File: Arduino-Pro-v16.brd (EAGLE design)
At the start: 100 x 80 mm, 36 parts, among them IC1 ATMEGA1281-16AU, IC2 MCP170312MB, J1 FTDI Basic Programmer

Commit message: Started ordering the layout of the board
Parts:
- removed FRAME1: FRAME-LETTER, SparkFun-Aesthetics:CREATIVE_COMMONS
- moved IC2 378.9 mm to (14.0, 68.6)
- moved JTAG_CONNECTOR 376.8 mm to (39.4, 69.8), turned to 180 degrees
- moved J2 370.5 mm to (62.2, 33.0)
- moved C4 361.5 mm to (45.7, 38.1), turned to 90 degrees
- moved J1 357.2 mm to (2.54, 50.8), turned to 90 degrees
- moved U$1 342.5 mm to (52.1, 41.9)
- moved R5 271.5 mm to (44.5, 41.9), turned to 180 degrees
- moved R4 270.4 mm to (44.5, 44.5), turned to 180 degrees
- moved R2 269.2 mm to (44.5, 47.0), turned to 180 degrees
- moved R1 268.1 mm to (44.5, 49.5), turned to 180 degrees
- moved LED5 263.6 mm to (40.6, 49.5), turned to 270 degrees
- moved LED4 259.6 mm to (40.6, 47.0), turned to 270 degrees
- moved LED3 255.7 mm to (40.6, 44.5), turned to 270 degrees
- moved T1 255.6 mm to (62.2, 38.1)
- moved D1 252.8 mm to (61.0, 43.2)
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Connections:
- removed net N$18: PWM3.1
- removed net N$19: PWM3.2
- removed net N$20: PWM3.3
- net PWM3A: now also PWM3.1
- net PWM3B: now also PWM3.2
- net PWM3C: now also PWM3.3

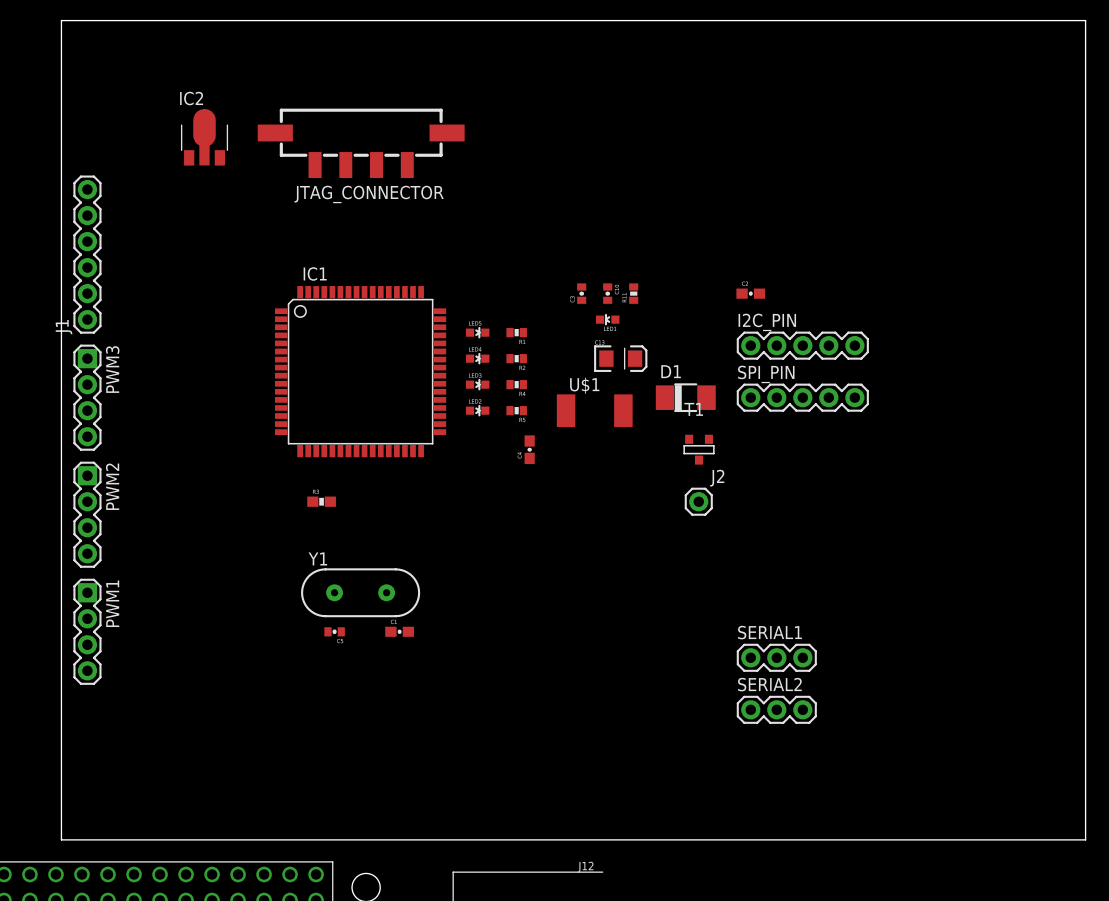
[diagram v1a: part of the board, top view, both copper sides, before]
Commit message: continued working on board layout, added ground plan polygon
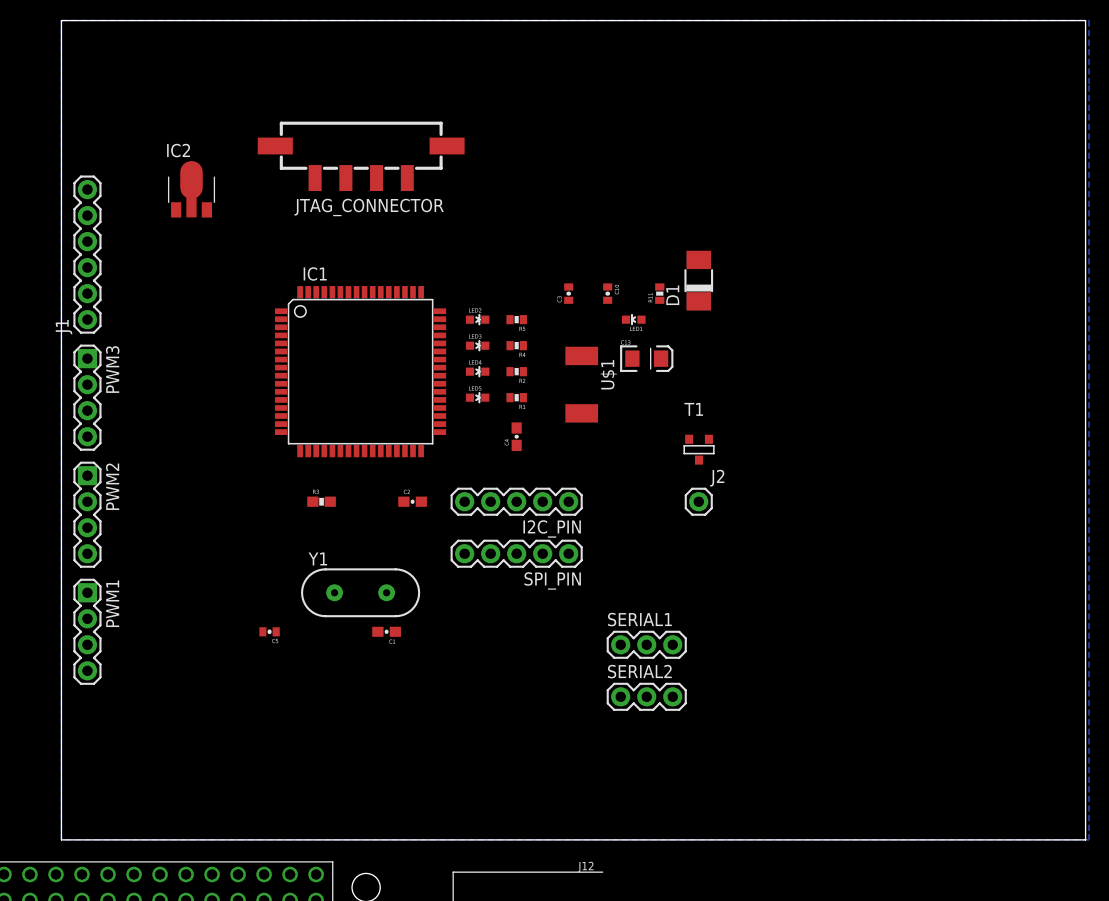
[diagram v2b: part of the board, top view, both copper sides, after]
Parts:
- moved C2 38.8 mm to (34.3, 33.0)
- moved SPI_PIN 23.4 mm to (49.5, 27.9), turned to 180 degrees
- moved I2C_PIN 23.4 mm to (49.5, 33.0), turned to 180 degrees
- moved SERIAL1 12.8 mm to (54.6, 19.1)
- moved SERIAL2 12.8 mm to (54.6, 14.0)
- moved D1 11.5 mm to (62.2, 54.6), turned to 90 degrees
- moved LED2 8.89 mm to (40.6, 50.8)
- moved R5 8.89 mm to (44.5, 50.8)
- moved C5 6.35 mm to (20.3, 20.3)
- moved LED5 6.35 mm to (40.6, 43.2)
- moved R1 6.35 mm to (44.5, 43.2)
- moved IC2 5.24 mm to (12.7, 63.5)
- moved LED3 3.81 mm to (40.6, 48.3)
- moved R4 3.81 mm to (44.5, 48.3)
- moved U$1 2.84 mm to (50.8, 44.5), turned to 270 degrees
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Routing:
- added copper zone on layer 16, net GND
